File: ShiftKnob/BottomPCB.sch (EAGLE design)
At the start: 37 parts, among them IC2 UA78M05DCY, J1 AVR_SPI_PRG_6PTH, Q1 16MHz, Q2 MOSFET-NCHANNELSMD, Q3 MOSFET-PCHANNELSMD, Q4 MOSFET-NCHANNELSMD, Q5 MOSFET-NCHANNELSMD, Q6 MOSFET-NCHANNELSMD, U1 ATMEGA328, U3 FT232RL-BASICSSOP

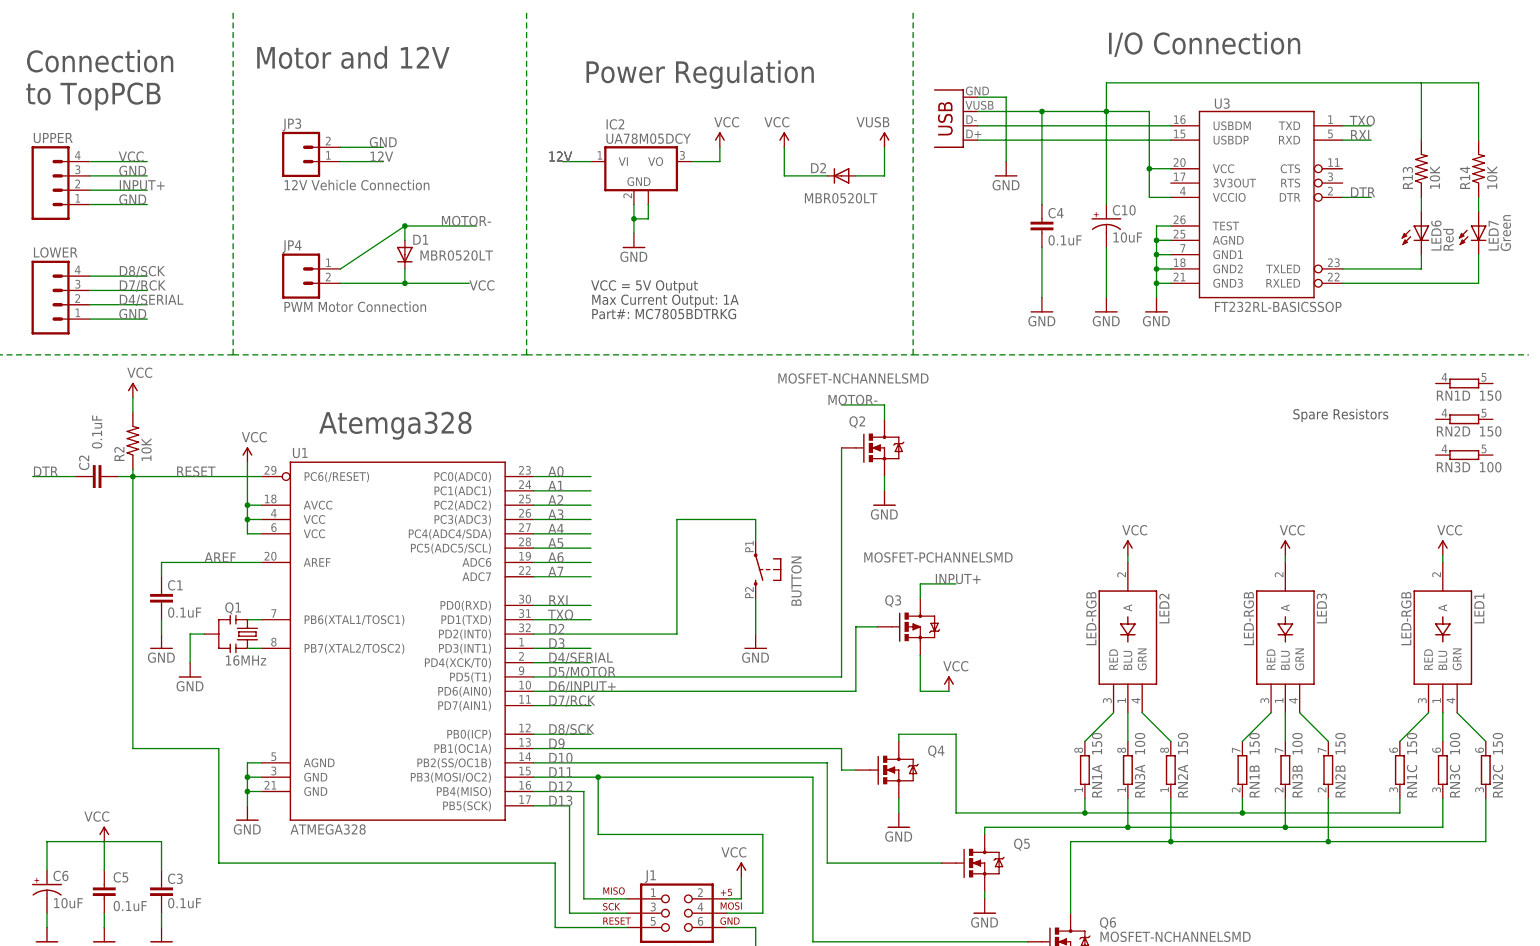
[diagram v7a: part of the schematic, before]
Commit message: swap pins on motor connection. add junctions where necessary. reorganize resistors for easier board layout.
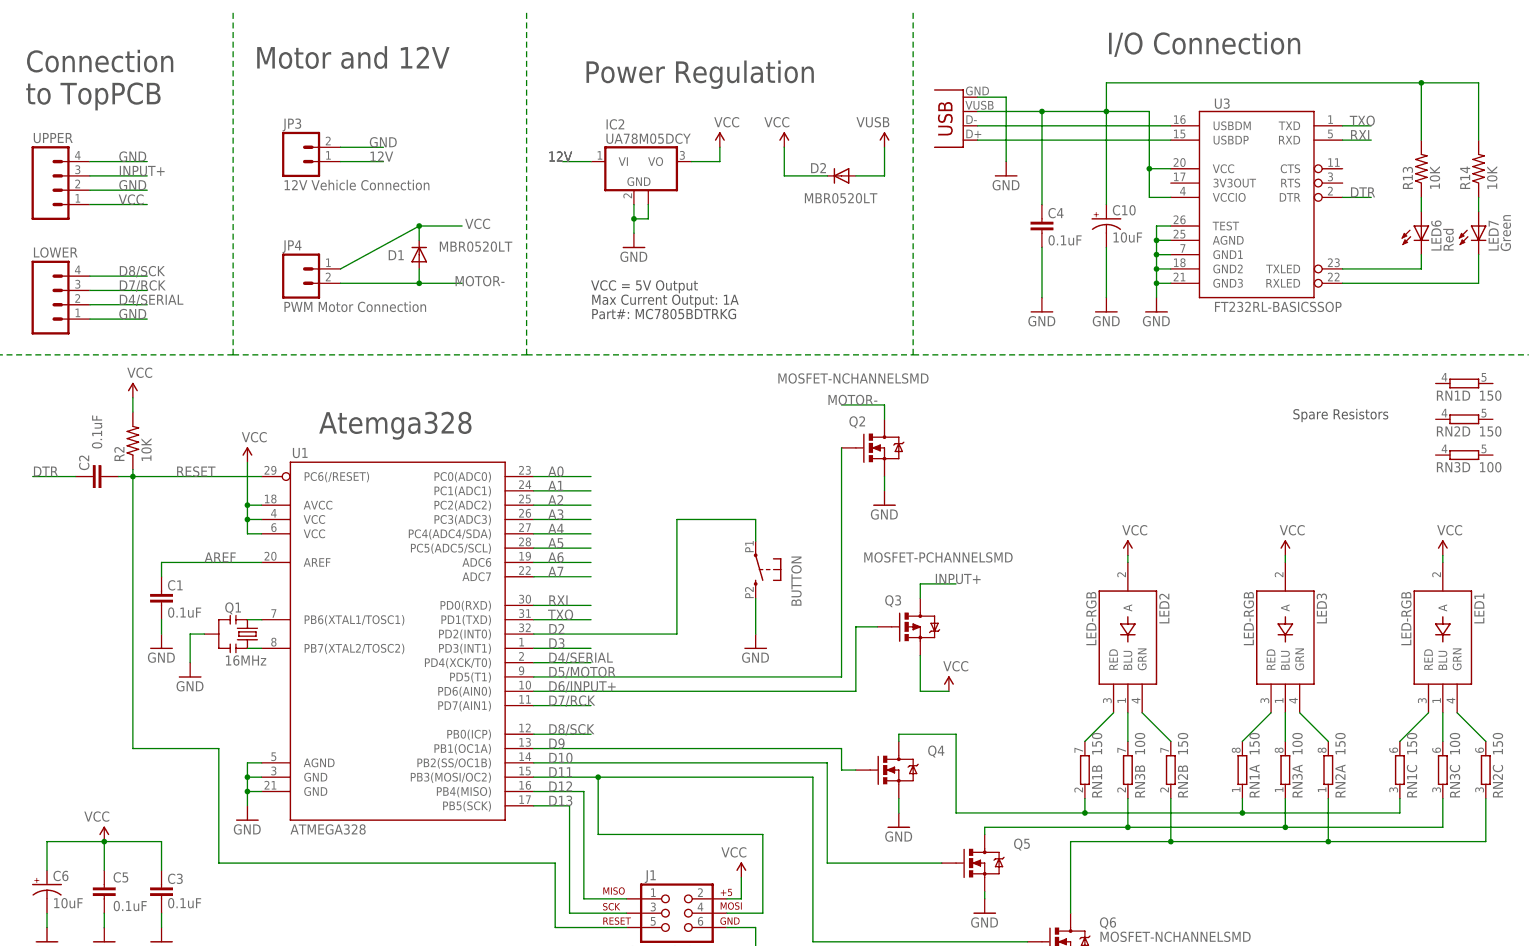
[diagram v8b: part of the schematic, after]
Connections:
- removed net N$25: LED2.BLU, RN3A.2
- new net N$20: LED3.BLU, RN3A.2
- net GND: now also UPPER.2, UPPER.4; no longer UPPER.1, UPPER.3
- net INPUT+: now also UPPER.3; no longer UPPER.2
- net MOTOR-: now also JP4.1; no longer JP4.2
- net N$16: now also LED2.BLU; no longer LED3.BLU
- net N$4: now also RN1B.2; no longer RN1A.2
- net N$5: now also RN2B.2; no longer RN2A.2
- net N$6: now also RN1A.2; no longer RN1B.2
- net N$8: now also RN2A.2; no longer RN2B.2
- net VCC: now also JP4.2, UPPER.1; no longer JP4.1, UPPER.4
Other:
- moved on the sheet: D1, RN1A, RN1B, RN2A, RN2B, RN3A, RN3B
